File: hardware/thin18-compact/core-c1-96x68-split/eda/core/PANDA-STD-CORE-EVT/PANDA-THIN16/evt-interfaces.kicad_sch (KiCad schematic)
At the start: 5 parts, among them J302 SM03B-SRSS-TB NTC

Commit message: hw: prepare split-board sourcing, mechanical envelope and EVT plan
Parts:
- C301: LCSC (none) -> C6048128

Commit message: hw: correct prototype footprints and prepare Split-C1 JLC CAM handoff
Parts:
- C301: footprint Capacitor_SMD:C_1210_3225Metric -> panda-standard:CPH3225A_Polarized_Derived

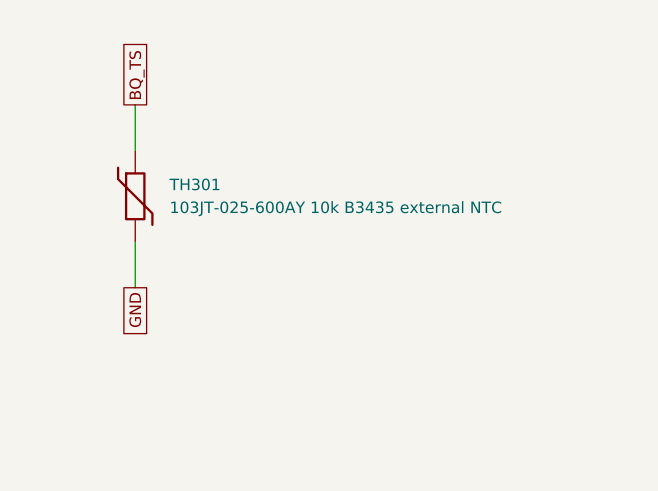
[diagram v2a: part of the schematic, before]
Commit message: hw: apply reviewed domestic ECOs and gate incomplete Split-C1 orders
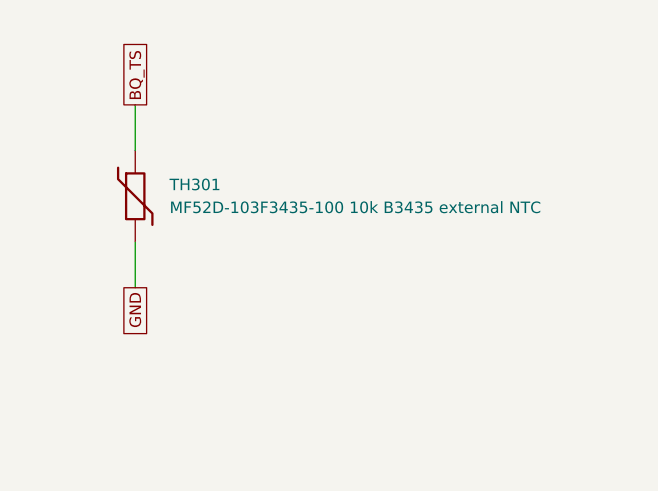
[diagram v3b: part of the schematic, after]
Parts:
- R615: LCSC C23068 -> C140082; MPN 0603WAF5231T5E -> RS-03K5231FT; Manufacturer UNI-ROYAL -> FH (Fenghua Advanced)
- R616: LCSC C23000 -> C321843; MPN 0603WAF3012T5E -> RS-03K3012FT; Manufacturer UNI-ROYAL -> FH (Fenghua Advanced)
- TH301: value 103JT-025-600AY 10k B3435 external NTC -> MF52D-103F3435-100 10k B3435 external NTC; LCSC (none) -> C394023; MPN 103JT-025-600AY -> MF52D-103F3435-100; Manufacturer SEMITEC -> Nanjing Shiheng Elec

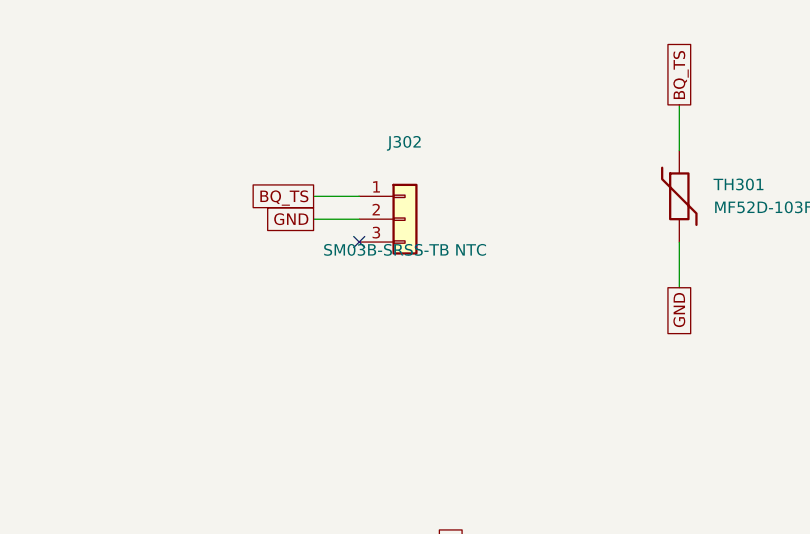
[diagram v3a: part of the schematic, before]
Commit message: hw: apply domestic wire, FPC and inductor ECOs with replay guards
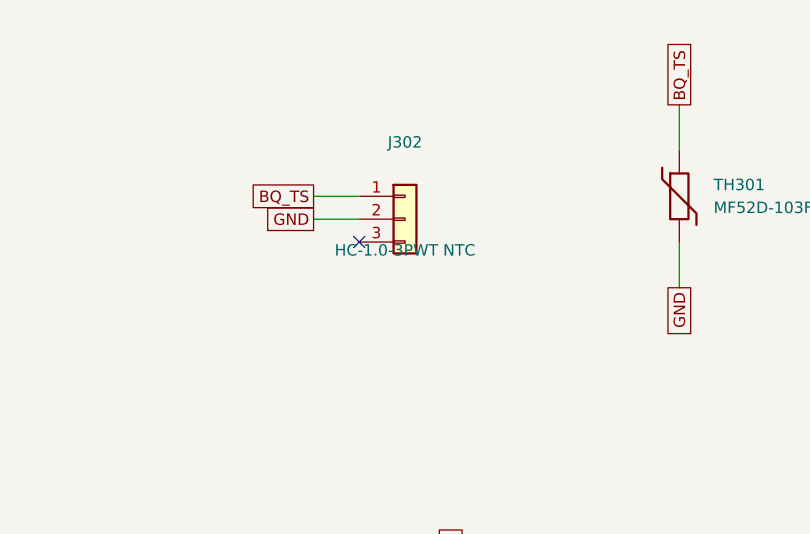
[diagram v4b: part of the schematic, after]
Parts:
- J302: value SM03B-SRSS-TB NTC -> HC-1.0-3PWT NTC; footprint Connector_JST:JST_SH_SM03B-SRSS-TB_1x03-1MP_P1.00mm_Horizontal -> panda-standard:HCTL_HC10_3PWT; LCSC C160403 -> C2845362; MPN SM03B-SRSS-TB(LF)(SN) -> HC-1.0-3PWT; Manufacturer JST -> HCTL

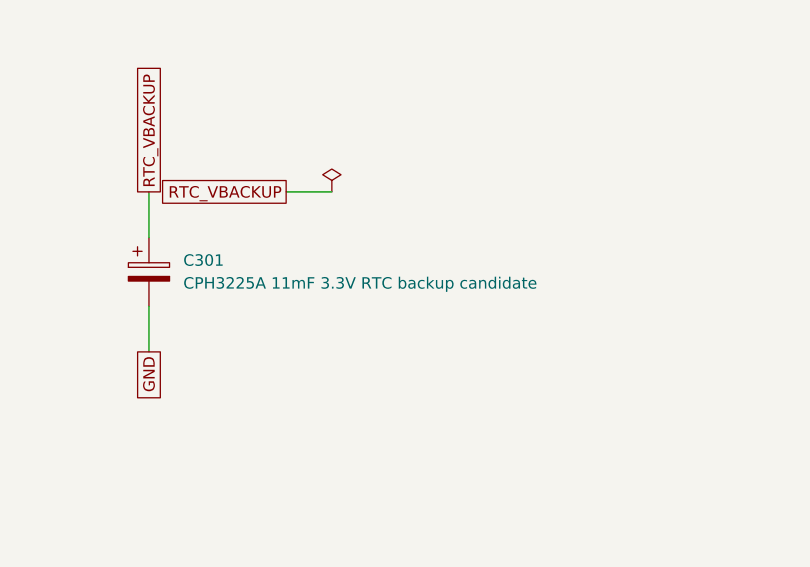
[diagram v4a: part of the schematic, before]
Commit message: hw: complete Split-C1 domestic RTC backup and EPD MOS ECO
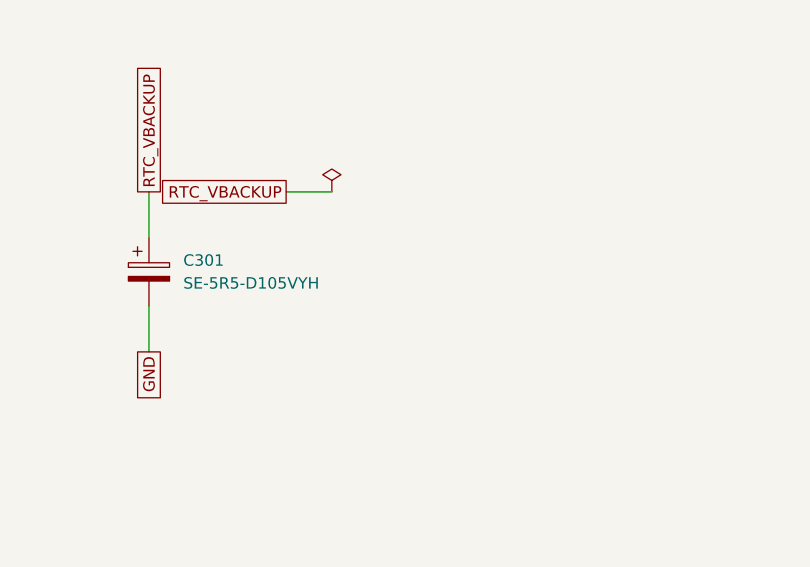
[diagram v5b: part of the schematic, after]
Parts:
- C301: value CPH3225A 11mF 3.3V RTC backup candidate -> SE-5R5-D105VYH; footprint panda-standard:CPH3225A_Polarized_Derived -> panda-standard:KAMCAP_SE5R5_D105VYH; LCSC C6048128 -> C118887; MPN CPH3225A -> SE-5R5-D105VYH; Manufacturer Seiko Instruments -> KAMCAP

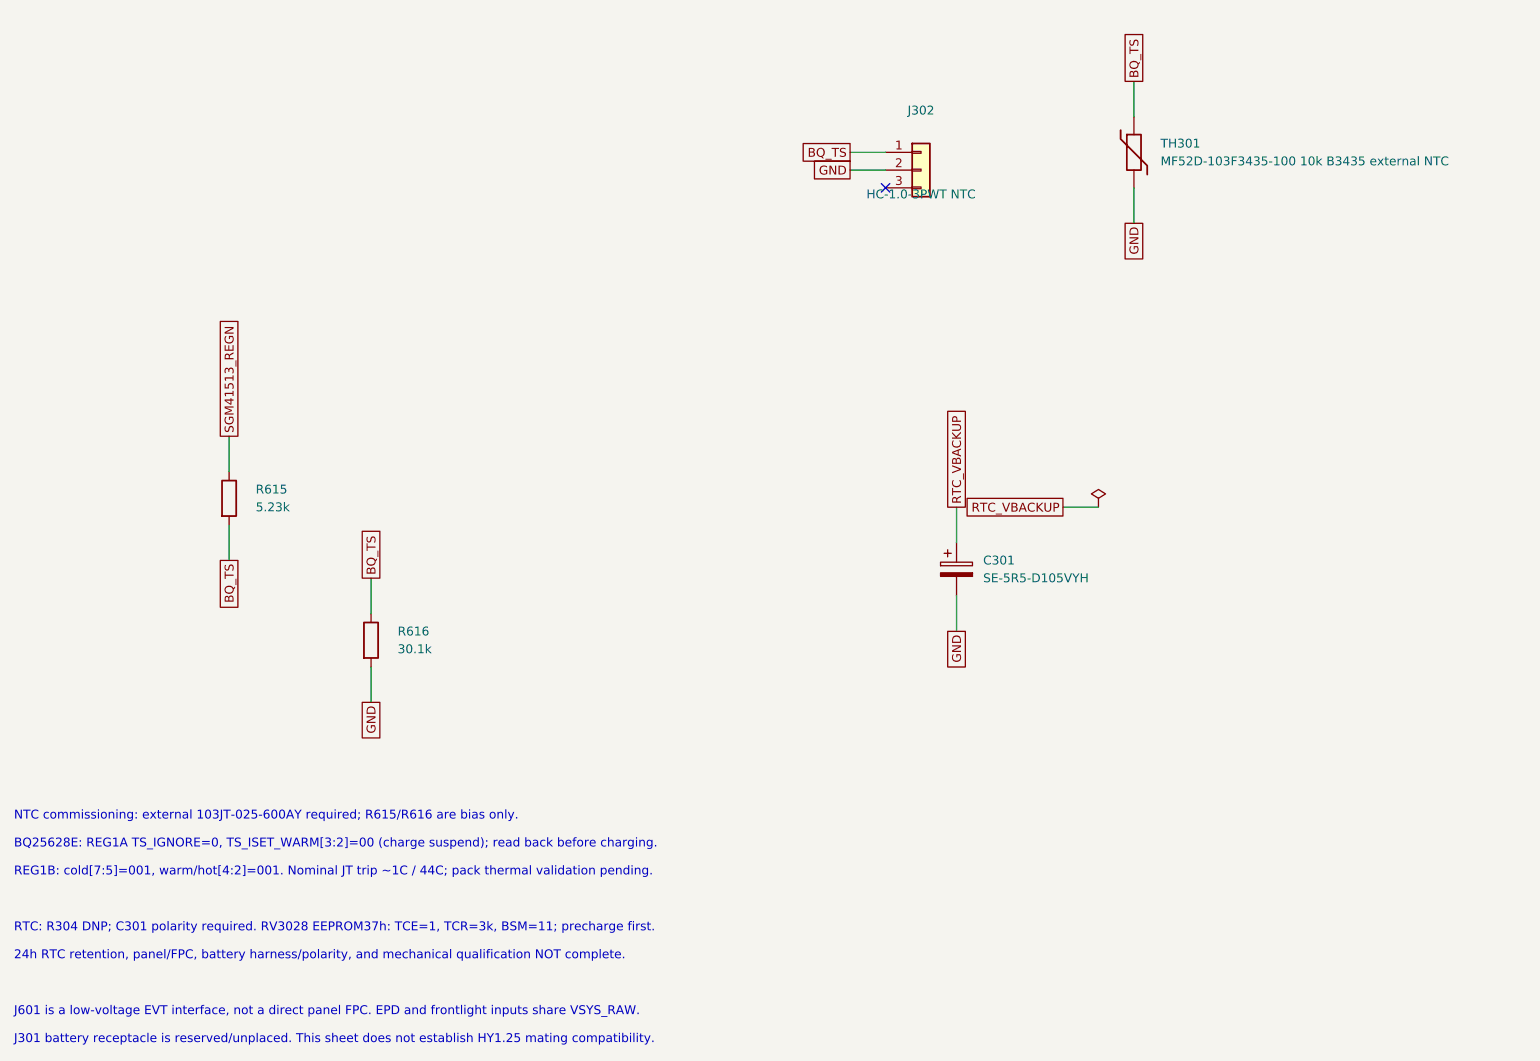
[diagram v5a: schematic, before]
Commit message: fix(hardware): use exact H3C capacitor with 20mm leads
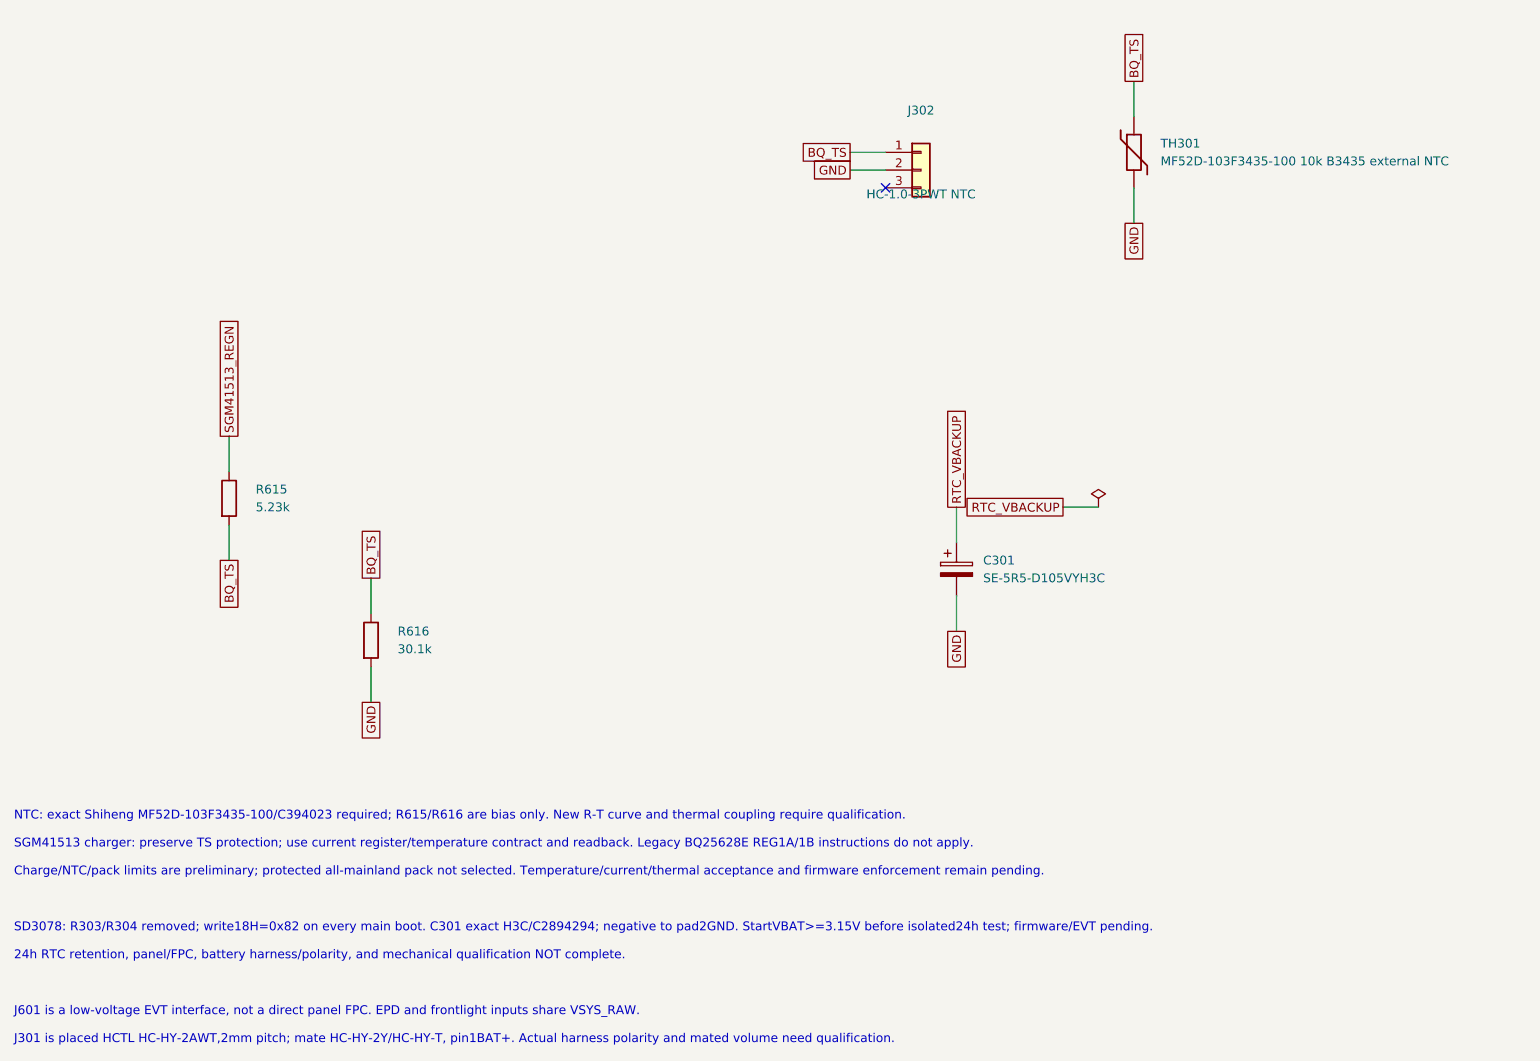
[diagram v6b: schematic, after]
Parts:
- C301: value SE-5R5-D105VYH -> SE-5R5-D105VYH3C; footprint panda-standard:KAMCAP_SE5R5_D105VYH -> panda-standard:KAMCAP_SE5R5_D105VYH3C; LCSC C118887 -> C2894294; MPN SE-5R5-D105VYH -> SE-5R5-D105VYH3C
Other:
- note added: "Charge/NTC/pack limits are preliminary; protected all-mainland pack not selected. Temperature/current/thermal acceptance and firmware enforcement remain pending."
- note added: "J301 is placed HCTL HC-HY-2AWT,2mm pitch; mate HC-HY-2Y/HC-HY-T, pin1BAT+. Actual harness polarity and mated volume need qualification."
- note added: "NTC: exact Shiheng MF52D-103F3435-100/C394023 required; R615/R616 are bias only. New R-T curve and thermal coupling require qualification."
- note added: "SD3078: R303/R304 removed; write18H=0x82 on every main boot. C301 exact H3C/C2894294; negative to pad2GND. StartVBAT>=3.15V before isolated24h test; firmware/EVT pending."
- note added: "SGM41513 charger: preserve TS protection; use current register/temperature contract and readback. Legacy BQ25628E REG1A/1B instructions do not apply."
- note removed: "BQ25628E: REG1A TS_IGNORE=0, TS_ISET_WARM[3:2]=00 (charge suspend); read back before charging."
- note removed: "J301 battery receptacle is reserved/unplaced. This sheet does not establish HY1.25 mating compatibility."
- note removed: "NTC commissioning: external 103JT-025-600AY required; R615/R616 are bias only."
- note removed: "REG1B: cold[7:5]=001, warm/hot[4:2]=001. Nominal JT trip ~1C / 44C; pack thermal validation pending."
- note removed: "RTC: R304 DNP; C301 polarity required. RV3028 EEPROM37h: TCE=1, TCR=3k, BSM=11; precharge first."
